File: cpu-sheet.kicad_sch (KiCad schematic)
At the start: 52 parts, among them J3 GPIO_HEADER, J5 USB_B_Micro, J6 PROG_CONN, SW1 RESET, U11 CH340G, U6 SRV05-4, U7 23LC1024, U8 STM32L432KC, U9 SRV05-4, Y2 32.768K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

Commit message: RX and TX leds together, minor layout & silk fixes etc
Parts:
- removed SW1: RESET, Connector_PinHeader_2.54mm:PinHeader_1x02_P2.54mm_Horizontal, symbol Switch:SW_Push
- added J4: GPIOR_HEADER, Connector_PinHeader_2.54mm:PinHeader_1x05_P2.54mm_Vertical_SMD_Pin1Left, symbol Connector:Conn_01x05_Male
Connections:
- net GND: now also J4.5 (Pin_5)
- net at C54.2, R26.2: now also J4.4 (Pin_4)
- new net GPIOR1: J4.1 (Pin_1)
- new net GPIOR2: J4.2 (Pin_2)
- new net GPIOR3: J4.3 (Pin_3)
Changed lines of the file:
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@@
+    (stroke (width 0) (type default) (color 0 0 0 0))
+  )
+  (wire (pts (xy 48.26 57.15) (xy 50.8 57.15))
     (stroke (width 0) (type default) (color 0 0 0 0))
   )
@@
     (stroke (width 0) (type default) (color 0 0 0 0))
   )
-  (wire (pts (xy 62.23 54.61) (xy 62.23 64.77))
-    (stroke (width 0) (type default) (color 0 0 0 0))
-  )
   (wire (pts (xy 76.2 80.01) (xy 71.12 85.09))
     (stroke (width 0) (type default) (color 0 0 0 0))
@@
     (stroke (width 0) (type default) (color 0 0 0 0))
   )
+  (wire (pts (xy 48.26 59.69) (xy 50.8 59.69))
+    (stroke (width 0) (type default) (color 0 0 0 0))
+  )
   (wire (pts (xy 82.55 95.25) (xy 85.09 95.25))
     (stroke (width 0) (type default) (color 0 0 0 0))
@@
     (stroke (width 0) (type default) (color 0 0 0 0))
   )
+  (wire (pts (xy 48.26 64.77) (xy 62.23 64.77))
+    (stroke (width 0) (type default) (color 0 0 0 0))
+  )
   (wire (pts (xy 137.16 153.67) (xy 133.35 153.67))
     (stroke (width 0) (type default) (color 0 0 0 0))
   )
+  (wire (pts (xy 63.5 54.61) (xy 72.39 54.61))
+    (stroke (width 0) (type default) (color 0 0 0 0))
+  )
   (wire (pts (xy 90.17 147.32) (xy 90.17 148.59))
     (stroke (width 0) (type default) (color 0 0 0 0))
@@
     (stroke (width 0) (type default) (color 0 0 0 0))
   )
+  (wire (pts (xy 48.26 62.23) (xy 63.5 62.23))
+    (stroke (width 0) (type default) (color 0 0 0 0))
+  )
   (wire (pts (xy 110.49 97.79) (xy 118.11 97.79))
     (stroke (width 0) (type default) (color 0 0 0 0))
@@
     (stroke (width 0) (type default) (color 0 0 0 0))
   )
+  (wire (pts (xy 63.5 62.23) (xy 63.5 54.61))
+    (stroke (width 0) (type default) (color 0 0 0 0))
+  )
   (wire (pts (xy 101.6 153.67) (xy 101.6 147.32))
     (stroke (width 0) (type default) (color 0 0 0 0))
@@
   )
   (wire (pts (xy 97.79 107.95) (xy 97.79 105.41))
+    (stroke (width 0) (type default) (color 0 0 0 0))
+  )
+  (wire (pts (xy 48.26 54.61) (xy 50.8 54.61))
     (stroke (width 0) (type default) (color 0 0 0 0))
   )
@@
     )
   )
+  (global_label "GPIOR1" (shape output) (at 50.8 54.61 0) (fields_autoplaced)
+    (effects (font (size 1.0038 1.0038)) (justify left))
+    (property "Intersheet References" "${INTERSHEET_REFS}" (id 0) (at 58.134 54.5473 0)
+      (effects (font (size 1.0038 1.0038)) (justify left) hide)
+    )
+  )
   (global_label "GPIO_11" (shape bidirectional) (at 168.91 119.38 180) (fields_autoplaced)
     (effects (font (size 1.27 1.27)) (justify right))
@@
     )
   )
+  (global_label "GPIOR2" (shape output) (at 50.8 57.15 0) (fields_autoplaced)
+    (effects (font (size 1.0038 1.0038)) (justify left))
+    (property "Intersheet References" "${INTERSHEET_REFS}" (id 0) (at 58.134 57.0873 0)
+      (effects (font (size 1.0038 1.0038)) (justify left) hide)
+    )
+  )
   (global_label "GPIO10_TERMINAL" (shape bidirectional) (at 204.47 105.41 0) (fields_autoplaced)
     (effects (font (size 1.27 1.27)) (justify left))
@@
     (property "Intersheet References" "${INTERSHEET_REFS}" (id 0) (at 0 0 0)
       (effects (font (size 1.27 1.27)) hide)
+    )
+  )
+  (global_label "GPIOR3" (shape output) (at 50.8 59.69 0) (fields_autoplaced)
+    (effects (font (size 1.0038 1.0038)) (justify left))
+    (property "Intersheet References" "${INTERSHEET_REFS}" (id 0) (at 58.134 59.6273 0)
+      (effects (font (size 1.0038 1.0038)) (justify left) hide)
     )
   )
@@
     )
     (pin "1")
-  )
-  (symbol (lib_id "Switch:SW_Push") (at 67.31 54.61 0) (unit 1)
-    (in_bom yes) (on_board yes)
-    (property "Reference" "SW1" (id 0) (at 67.31 47.371 0))
-    (property "Value" "RESET" (id 1) (at 67.31 49.6824 0))
-    (property "Footprint" "Connector_PinHeader_2.54mm:PinHeader_1x02_P2.54mm_Horizontal" (id 2) (at 67.31 49.53 0)
-      (effects (font (size 1.27 1.27)) hide)
-    )
-    (property "Datasheet" "~" (id 3) (at 67.31 49.53 0)
-      (effects (font (size 1.27 1.27)) hide)
-    )
-    (property "LCSC" "C376120" (id 4) (at 67.31 54.61 0)
-      (effects (font (size 1.27 1.27)) hide)
-    )
-    (pin "1")
-    (pin "2")
   )
   (symbol (lib_id "Device:R_Small") (at 130.81 64.77 0) (unit 1)
@@
     (pin "1")
   )
+  (symbol (lib_id "Connector:Conn_01x05_Male") (at 43.18 59.69 0) (unit 1)
+    (in_bom yes) (on_board yes)
+    (property "Reference" "J4" (id 0) (at 41.91 50.8 0))
+    (property "Value" "GPIOR_HEADER" (id 1) (at 43.18 67.31 0))
+    (property "Footprint" "Connector_PinHeader_2.54mm:PinHeader_1x05_P2.54mm_Vertical_SMD_Pin1Left" (id 2) (at 43.18 59.69 0)
+      (effects (font (size 1.27 1.27)) hide)
+    )
+    (property "Datasheet" "~" (id 3) (at 43.18 59.69 0)
+      (effects (font (size 1.27 1.27)) hide)
+    )
+    (property "LCSC" "C780063" (id 4) (at 43.18 59.69 0)
+      (effects (font (size 1.27 1.27)) hide)
+    )
+    (pin "1")
+    (pin "2")
+    (pin "3")
+    (pin "4")
+    (pin "5")
+  )
 )

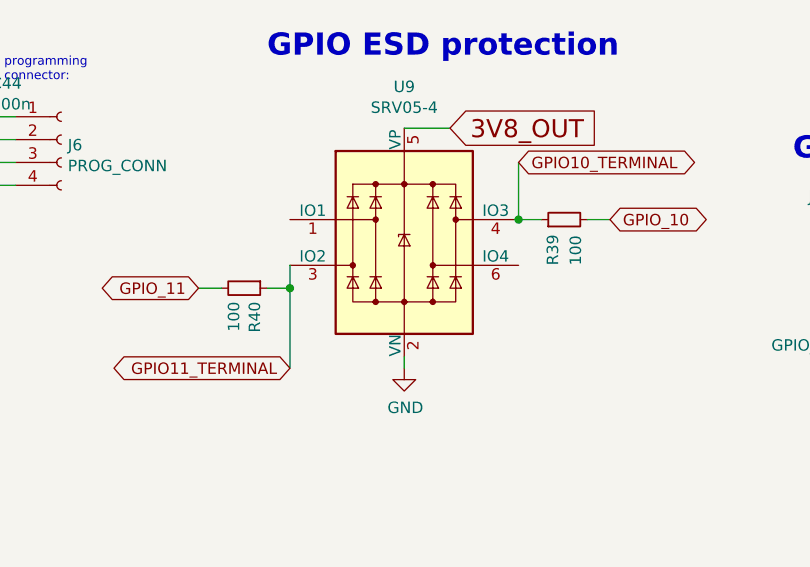
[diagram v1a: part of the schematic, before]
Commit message: 50R to 2*100R in parallel to use JLC Basic, 2kV cap to SMD to avoid THD placement cost, silk enhancements, added missing LCSC codes
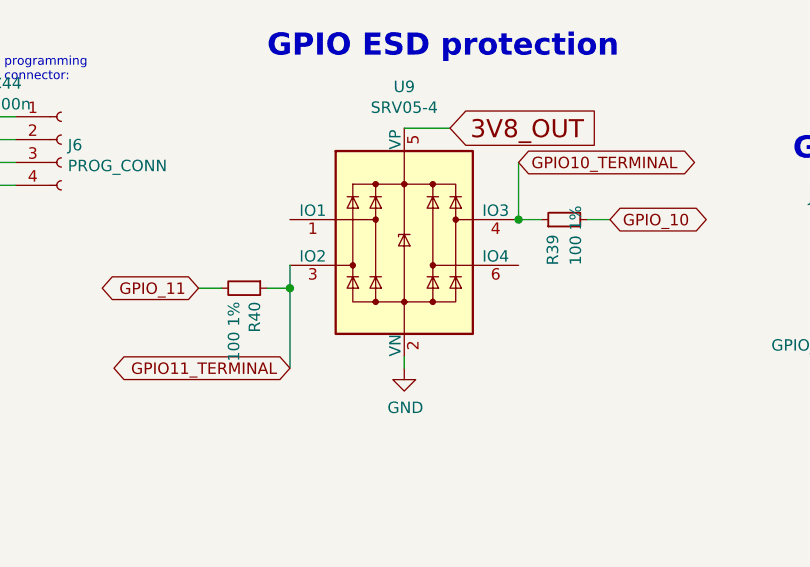
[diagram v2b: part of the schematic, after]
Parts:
- R39, R40: value 100 -> 100 1%
- U8: DNP TRUE -> (none); LCSC (none) -> C1337280
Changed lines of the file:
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@@
       (effects (font (size 1.27 1.27)) (justify left))
     )
-    (property "Value" "100" (id 1) (at 210.82 116.84 0)
+    (property "Value" "100 1%" (id 1) (at 210.82 116.84 0)
       (effects (font (size 1.27 1.27)) (justify left))
     )
@@
       (effects (font (size 1.27 1.27)) (justify left))
     )
-    (property "Value" "100" (id 1) (at 172.847 120.8786 0)
+    (property "Value" "100 1%" (id 1) (at 172.847 120.8786 0)
       (effects (font (size 1.27 1.27)) (justify left))
     )
@@
       (effects (font (size 1.27 1.27)) hide)
     )
-    (property "DNP" "TRUE" (id 4) (at 97.79 80.01 0)
+    (property "DNP" "" (id 4) (at 97.79 80.01 0)
       (effects (font (size 1.27 1.27)) hide)
     )
+    (property "LCSC" "C1337280" (id 5) (at 97.79 80.01 0)
+      (effects (font (size 1.27 1.27)) hide)
+    )

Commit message: misc
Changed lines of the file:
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@@
     (stroke (width 0) (type default) (color 0 0 0 0))
   )
-  (wire (pts (xy 91.44 138.43) (xy 104.14 138.43))
+  (wire (pts (xy 100.33 138.43) (xy 104.14 138.43))
     (stroke (width 0) (type default) (color 0 0 0 0))
   )
@@
   )
   (global_label "3V3_CPU" (shape input) (at 248.92 39.37 0) (fields_autoplaced)
-    (effects (font (size 2.0066 2.0066)) (justify left))
-    (property "Intersheet References" "${INTERSHEET_REFS}" (id 0) (at 0 0 0)
-      (effects (font (size 1.27 1.27)) hide)
+    (effects (font (size 2.0066 2.0066) (thickness 0.4013) bold) (justify left))
+    (property "Intersheet References" "${INTERSHEET_REFS}" (id 0) (at 266.0792 39.1694 0)
+      (effects (font (size 2.0066 2.0066) (thickness 0.4013) bold) (justify left) hide)
     )
   )
@@
   )
   (global_label "3V8_OUT" (shape input) (at 250.19 123.19 0) (fields_autoplaced)
-    (effects (font (size 2.0066 2.0066)) (justify left))
-    (property "Intersheet References" "${INTERSHEET_REFS}" (id 0) (at 0 0 0)
-      (effects (font (size 1.27 1.27)) hide)
+    (effects (font (size 2.0066 2.0066) (thickness 0.4013) bold) (justify left))
+    (property "Intersheet References" "${INTERSHEET_REFS}" (id 0) (at 266.967 122.9894 0)
+      (effects (font (size 2.0066 2.0066) (thickness 0.4013) bold) (justify left) hide)
     )
   )
   (global_label "3V3_CPU" (shape input) (at 46.99 44.45 180) (fields_autoplaced)
-    (effects (font (size 2.0066 2.0066)) (justify right))
-    (property "Intersheet References" "${INTERSHEET_REFS}" (id 0) (at 0 0 0)
-      (effects (font (size 1.27 1.27)) hide)
+    (effects (font (size 2.0066 2.0066) (thickness 0.4013) bold) (justify right))
+    (property "Intersheet References" "${INTERSHEET_REFS}" (id 0) (at 29.8308 44.2494 0)
+      (effects (font (size 2.0066 2.0066) (thickness 0.4013) bold) (justify right) hide)
     )
   )
@@
     )
   )
-  (global_label "3V3_CPU" (shape input) (at 91.44 138.43 180) (fields_autoplaced)
-    (effects (font (size 2.0066 2.0066)) (justify right))
-    (property "Intersheet References" "${INTERSHEET_REFS}" (id 0) (at 0 0 0)
-      (effects (font (size 1.27 1.27)) hide)
+  (global_label "3V3_CPU" (shape input) (at 100.33 138.43 180) (fields_autoplaced)
+    (effects (font (size 1.5 1.5) (thickness 0.4013) bold) (justify right))
+    (property "Intersheet References" "${INTERSHEET_REFS}" (id 0) (at 87.3529 138.2425 0)
+      (effects (font (size 1.5 1.5) (thickness 0.4013) bold) (justify right) hide)
     )
   )
@@
   )
   (global_label "3V8_OUT" (shape input) (at 196.85 101.6 0) (fields_autoplaced)
-    (effects (font (size 2.0066 2.0066)) (justify left))
-    (property "Intersheet References" "${INTERSHEET_REFS}" (id 0) (at 0 0 0)
-      (effects (font (size 1.27 1.27)) hide)
+    (effects (font (size 1.5 1.5) (thickness 0.4013) bold) (justify left))
+    (property "Intersheet References" "${INTERSHEET_REFS}" (id 0) (at 209.5414 101.4125 0)
+      (effects (font (size 1.5 1.5) (thickness 0.4013) bold) (justify left) hide)
     )
   )
@@
   )
   (global_label "3V3_CPU" (shape input) (at 135.89 100.33 180) (fields_autoplaced)
-    (effects (font (size 2.0066 2.0066)) (justify right))
-    (property "Intersheet References" "${INTERSHEET_REFS}" (id 0) (at 0 0 0)
-      (effects (font (size 1.27 1.27)) hide)
-    )
-  )
+    (effects (font (size 1.5 1.5) (thickness 0.4013) bold) (justify right))
+    (property "Intersheet References" "${INTERSHEET_REFS}" (id 0) (at 122.9129 100.1425 0)
+      (effects (font (size 1.5 1.5) (thickness 0.4013) bold) (justify right) hide)
+    )
+  )

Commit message: return paste back to SAW as will be assembled
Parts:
- U7: DNP TRUE -> (none)
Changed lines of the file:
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@@
       (effects (font (size 1.524 1.524)))
     )
-    (property "DNP" "TRUE" (id 4) (at 203.2 43.18 0)
+    (property "DNP" "" (id 4) (at 203.2 43.18 0)
       (effects (font (size 1.27 1.27)) hide)
     )

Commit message: replaced out-of-stock components LCSC codes with new ones
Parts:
- R36, R37: LCSC C22843 -> C118397
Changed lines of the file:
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@@
       (effects (font (size 1.27 1.27)) hide)
     )
-    (property "LCSC" "C22843" (id 4) (at 189.23 73.66 0)
+    (property "LCSC" "C118397" (id 4) (at 189.23 73.66 0)
       (effects (font (size 1.27 1.27)) hide)
     )
@@
       (effects (font (size 1.27 1.27)) hide)
     )
-    (property "LCSC" "C22843" (id 4) (at 240.03 73.66 0)
+    (property "LCSC" "C118397" (id 4) (at 240.03 73.66 0)
       (effects (font (size 1.27 1.27)) hide)
     )

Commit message: LCSC codes changed (out-of-stock parts)
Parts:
- C55, C56: LCSC C424850 -> C519108
- J6: LCSC C225501 -> C124413
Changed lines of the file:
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@@
       (effects (font (size 1.27 1.27)) hide)
     )
-    (property "LCSC" "C424850" (id 4) (at 63.5 78.74 0)
+    (property "LCSC" "C519108" (id 4) (at 63.5 78.74 0)
       (effects (font (size 1.27 1.27)) hide)
     )
@@
       (effects (font (size 1.27 1.27)) hide)
     )
-    (property "LCSC" "C424850" (id 4) (at 63.5 85.09 0)
+    (property "LCSC" "C519108" (id 4) (at 63.5 85.09 0)
       (effects (font (size 1.27 1.27)) hide)
     )
@@
       (effects (font (size 1.27 1.27)) hide)
     )
-    (property "LCSC" "C225501" (id 4) (at 153.67 102.87 0)
-      (effects (font (size 1.27 1.27)) hide)
-    )
+    (property "LCSC" "C124413" (id 4) (at 153.67 102.87 0)
+      (effects (font (size 1.27 1.27)) hide)
+    )

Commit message: USB LED resistor -> 1.5k
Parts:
- R23: value 330 -> 1.5k; LCSC C23138 -> C118397
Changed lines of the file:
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@@
     (in_bom yes) (on_board yes)
     (property "Reference" "R23" (id 0) (at 54.61 139.8016 90))
-    (property "Value" "330" (id 1) (at 54.61 142.113 90))
+    (property "Value" "1.5k" (id 1) (at 54.61 142.113 90))
     (property "Footprint" "Resistor_SMD:R_0603_1608Metric" (id 2) (at 54.61 144.78 0)
       (effects (font (size 1.27 1.27)) hide)
@@
       (effects (font (size 1.27 1.27)) hide)
     )
-    (property "LCSC" "C23138" (id 4) (at 54.61 144.78 0)
+    (property "LCSC" "C118397" (id 4) (at 54.61 144.78 0)
       (effects (font (size 1.27 1.27)) hide)
     )

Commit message: added TX_LED resistor and legend for RF STATE HEADER (bottom)
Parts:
- added R45: 330, Resistor_SMD:R_0603_1608Metric, symbol Device:R_Small
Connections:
- net GPIOR3: now also R45.1; no longer J4.3 (Pin_3)
- new net: J4.3 (Pin_3), R45.2
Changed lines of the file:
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@@
     (stroke (width 0) (type default) (color 0 0 0 0))
   )
-  (wire (pts (xy 48.26 57.15) (xy 50.8 57.15))
+  (wire (pts (xy 48.26 57.15) (xy 54.61 57.15))
     (stroke (width 0) (type default) (color 0 0 0 0))
   )
@@
     (stroke (width 0) (type default) (color 0 0 0 0))
   )
+  (wire (pts (xy 53.34 59.69) (xy 54.61 59.69))
+    (stroke (width 0) (type default) (color 0 0 0 0))
+  )
   (wire (pts (xy 43.18 156.21) (xy 43.18 161.29))
     (stroke (width 0) (type default) (color 0 0 0 0))
@@
     (stroke (width 0) (type default) (color 0 0 0 0))
   )
-  (wire (pts (xy 48.26 59.69) (xy 50.8 59.69))
-    (stroke (width 0) (type default) (color 0 0 0 0))
-  )
   (wire (pts (xy 82.55 95.25) (xy 85.09 95.25))
     (stroke (width 0) (type default) (color 0 0 0 0))
@@
     (stroke (width 0) (type default) (color 0 0 0 0))
   )
-  (wire (pts (xy 48.26 54.61) (xy 50.8 54.61))
+  (wire (pts (xy 48.26 54.61) (xy 54.61 54.61))
     (stroke (width 0) (type default) (color 0 0 0 0))
   )
@@
     )
   )
-  (global_label "GPIOR1" (shape output) (at 50.8 54.61 0) (fields_autoplaced)
+  (global_label "GPIOR1" (shape output) (at 54.61 54.61 0) (fields_autoplaced)
     (effects (font (size 1.0038 1.0038)) (justify left))
-    (property "Intersheet References" "${INTERSHEET_REFS}" (id 0) (at 58.134 54.5473 0)
+    (property "Intersheet References" "${INTERSHEET_REFS}" (id 0) (at 61.944 54.5473 0)
       (effects (font (size 1.0038 1.0038)) (justify left) hide)
     )
@@
     )
   )
-  (global_label "GPIOR2" (shape output) (at 50.8 57.15 0) (fields_autoplaced)
+  (global_label "GPIOR2" (shape output) (at 54.61 57.15 0) (fields_autoplaced)
     (effects (font (size 1.0038 1.0038)) (justify left))
-    (property "Intersheet References" "${INTERSHEET_REFS}" (id 0) (at 58.134 57.0873 0)
+    (property "Intersheet References" "${INTERSHEET_REFS}" (id 0) (at 61.944 57.0873 0)
       (effects (font (size 1.0038 1.0038)) (justify left) hide)
     )
@@
     )
   )
-  (global_label "GPIOR3" (shape output) (at 50.8 59.69 0) (fields_autoplaced)
+  (global_label "GPIOR3" (shape output) (at 54.61 59.69 0) (fields_autoplaced)
     (effects (font (size 1.0038 1.0038)) (justify left))
-    (property "Intersheet References" "${INTERSHEET_REFS}" (id 0) (at 58.134 59.6273 0)
+    (property "Intersheet References" "${INTERSHEET_REFS}" (id 0) (at 61.944 59.6273 0)
       (effects (font (size 1.0038 1.0038)) (justify left) hide)
     )
@@
     (pin "1")
   )
+  (symbol (lib_id "Device:R_Small") (at 50.8 59.69 270) (unit 1)
+    (in_bom yes) (on_board yes)
+    (property "Reference" "R45" (id 0) (at 50.8 58.42 90))
+    (property "Value" "330" (id 1) (at 50.8 55.88 90))
+    (property "Footprint" "Resistor_SMD:R_0603_1608Metric" (id 2) (at 50.8 59.69 0)
+      (effects (font (size 1.27 1.27)) hide)
+    )
+    (property "Datasheet" "~" (id 3) (at 50.8 59.69 0)
+      (effects (font (size 1.27 1.27)) hide)
+    )
+    (property "LCSC" "C23138" (id 4) (at 50.8 59.69 0)
+      (effects (font (size 1.27 1.27)) hide)
+    )
+    (pin "1")
+    (pin "2")
+  )
   (symbol (lib_id "Connector:Conn_01x05_Male") (at 43.18 59.69 0) (unit 1)
